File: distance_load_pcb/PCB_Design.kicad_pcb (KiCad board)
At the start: 2 copper layers, 14 parts, among them J1 From Power Source 5V, J2 From Limit Switch (LS), J3 From Encoder (EC), J5 Screen_Front, J6 Screen_Back, J7 From Load Cell (LC), U1 ESP-01v090, U2 YAAJ_BluePill_Part_Like_SWD_B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

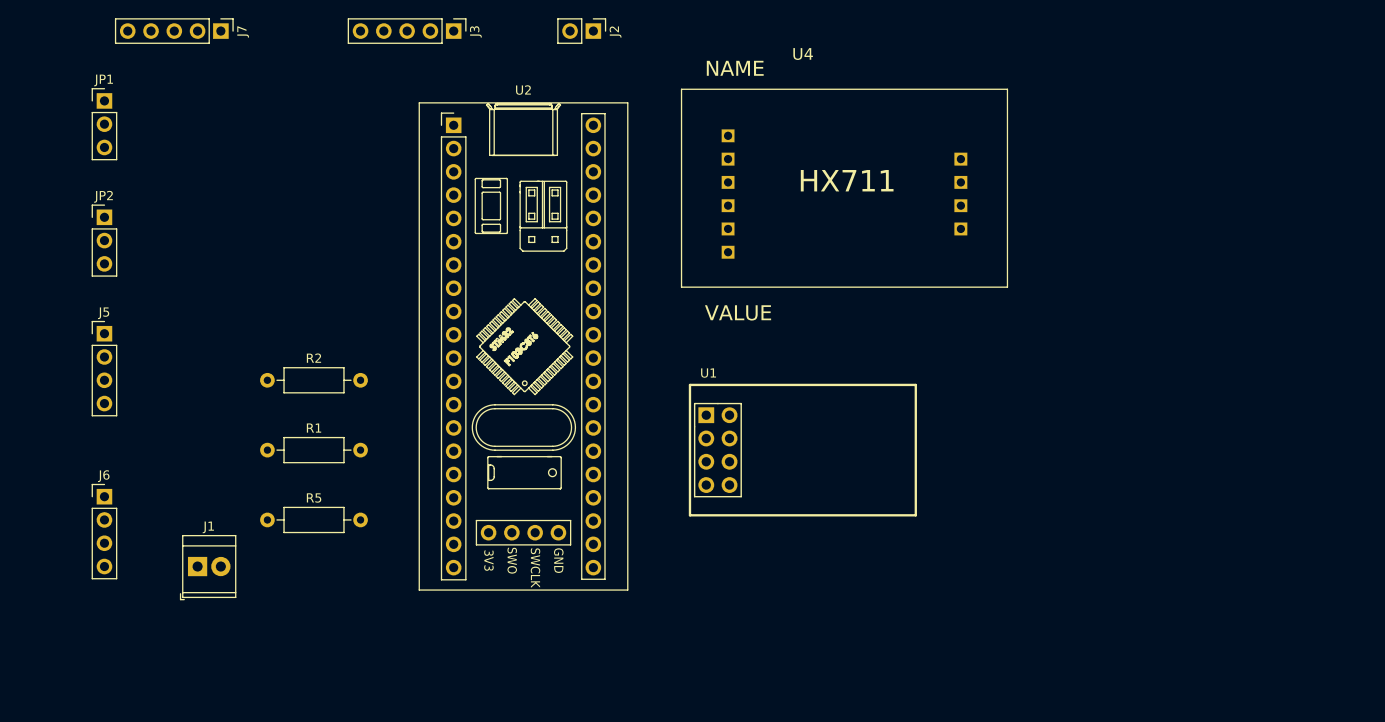
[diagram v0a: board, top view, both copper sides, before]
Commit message: finish pcb force and distance
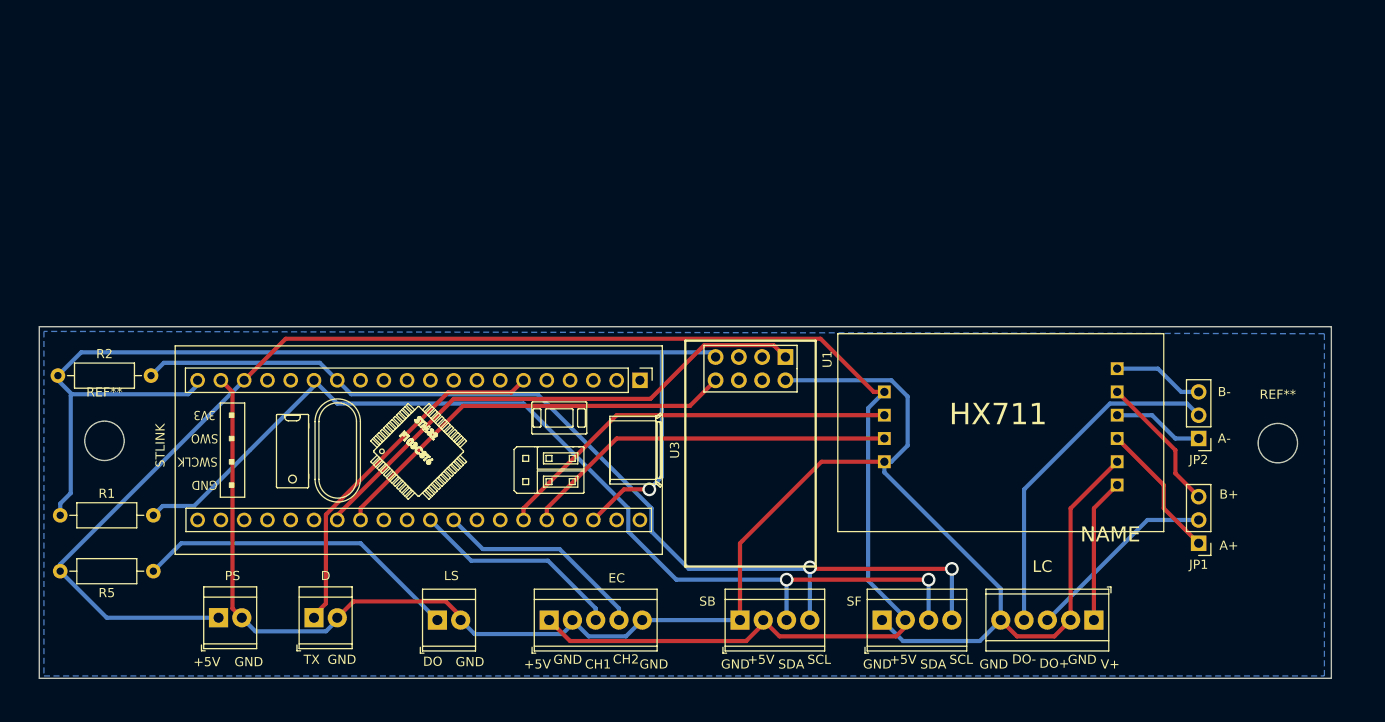
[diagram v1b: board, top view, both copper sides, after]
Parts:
- removed U2: YAAJ_BluePill_Part_Like_SWD_Breakout, Footprints:YAAJ_BluePill_SWD_1
- added D: Debug output, TerminalBlock_TE-Connectivity:TerminalBlock_TE_282834-2_1x02_P2.54mm_Horizontal, F.Cu at (99.1, 99.6)
- added REF**: MountingHole_4.3mm_M4, MountingHole:MountingHole_4.3mm_M4, F.Cu at (204.2, 80.5)
- added REF**: MountingHole_4.3mm_M4, MountingHole:MountingHole_4.3mm_M4, F.Cu at (76.2, 80.3)
- added U3: YAAJ_BluePill_Part_Like, Footprints:YAAJ_BluePill_1, F.Cu at (134.6, 73.7)
- EC: renamed from J3; footprint Connector_PinHeader_2.54mm:PinHeader_1x05_P2.54mm_Vertical -> TerminalBlock_TE-Connectivity:TerminalBlock_TE_282834-5_1x05_P2.54mm_Horizontal
- J7: footprint Connector_PinHeader_2.54mm:PinHeader_1x05_P2.54mm_Vertical -> TerminalBlock_TE-Connectivity:TerminalBlock_TE_282834-5_1x05_P2.54mm_Horizontal
- LS: renamed from J2; footprint Connector_PinHeader_2.54mm:PinHeader_1x02_P2.54mm_Vertical -> TerminalBlock_TE-Connectivity:TerminalBlock_TE_282834-2_1x02_P2.54mm_Horizontal
- SB: renamed from J6; footprint Connector_PinHeader_2.54mm:PinHeader_1x04_P2.54mm_Vertical -> TerminalBlock_TE-Connectivity:TerminalBlock_TE_282834-4_1x04_P2.54mm_Horizontal
- SF: renamed from J5; footprint Connector_PinHeader_2.54mm:PinHeader_1x04_P2.54mm_Vertical -> TerminalBlock_TE-Connectivity:TerminalBlock_TE_282834-4_1x04_P2.54mm_Horizontal
- moved JP1 128.8 mm to (195.6, 91.4), turned to 180 degrees
- moved JP2 121.8 mm to (195.6, 80.0), turned to 180 degrees
- moved J7 114.9 mm to (184.2, 99.8), turned to 180 degrees
- moved SF 90.4 mm to (161.0, 99.8)
- moved SB 70.6 mm to (145.5, 99.8)
- moved LS 66.5 mm to (112.5, 99.8), turned to 0 degrees
- moved EC 65.1 mm to (124.7, 99.8), turned to 0 degrees
- moved LC 63.6 mm to (195.6, 55.9), turned to 180 degrees
- moved R1 23.7 mm to (71.4, 88.4)
- moved R2 22.9 mm to (71.1, 73.2)
- moved R5 13.6 mm to (81.5, 94.5), turned to 180 degrees
- moved U1 10.7 mm to (150.5, 71.1), turned to -90 degrees
- moved PS 6.04 mm to (88.6, 99.6)
- renumbered U4 to LC, J1 to PS
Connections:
- net Shield_EC renamed GND
- EC pad 1: V+_EC -> +5V
- LC pad VCC: A_DEFINIR -> +5V
- U1 pad 1: USART1_TX -> USART2_TX
- U1 pad 8: USART1_RX -> USART2_RX
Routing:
- net GND: track 0.00 -> 203.7 mm
- net +5V: track 0.00 -> 192.9 mm
- net +3.3V: track 0.00 -> 127.1 mm, vias 0 -> 1
- net SDA1: track 0.00 -> 110.6 mm, vias 0 -> 2
- net SCL1: track 0.00 -> 110.2 mm, vias 0 -> 2
- net USART2_TX: track 0.00 -> 57.6 mm
- net USART2_RX: track 0.00 -> 45.8 mm
- net USART3_TX: track 0.00 -> 44.8 mm
- net USART3_RX: track 0.00 -> 41.3 mm
- net USART1_TX: track 0.00 -> 39.4 mm
- net DO-_LC: track 0.00 -> 38.2 mm
- net DO_LS: track 0.00 -> 35.7 mm
- net CH2-_EC: track 0.00 -> 23.3 mm
- net CH1_EC: track 0.00 -> 23.3 mm
- net DO+_LC: track 0.00 -> 21.0 mm
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- added copper zone on B.Cu, net GND
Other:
- board outline added: 141 x 38.4 mm
- board text added: "+5V"
- board text added: "A+"
- board text added: "A-"
- board text added: "B+"
- board text added: "B-"
- board text added: "CH1"
- board text added: "CH2"
- board text added: "DO"
- board text added: "DO+"
- board text added: "DO-"
- board text added: "GND"
- board text added: "SCL"
- board text added: "SDA"
- board text added: "STLINK"
- board text added: "TX"
- board text added: "V+"

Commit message: felipin's suggestions, all the tracs arrive at the components by the bottom
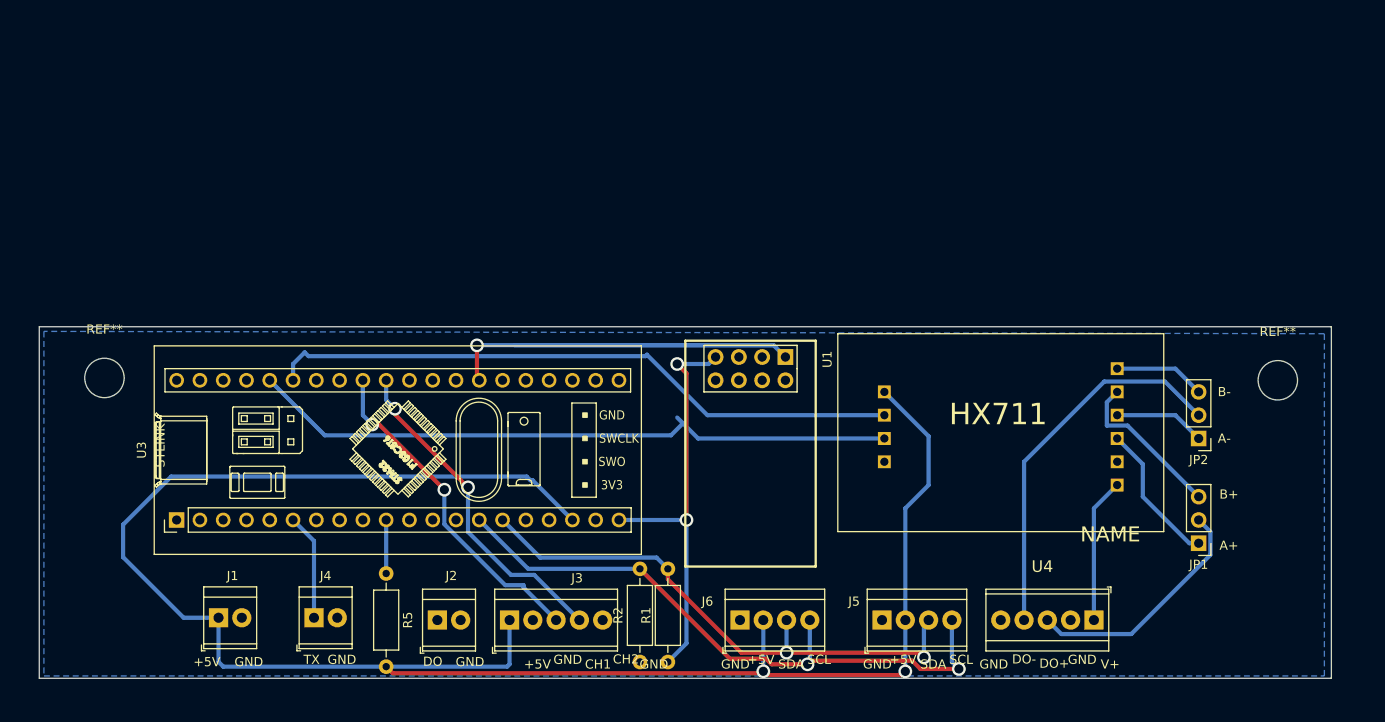
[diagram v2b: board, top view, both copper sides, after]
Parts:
- moved R2 70.8 mm to (134.6, 104.4), turned to 90 degrees
- moved R1 68.2 mm to (137.7, 104.4), turned to 90 degrees
- moved U3 52.8 mm to (84.1, 88.9), turned to 90 degrees
- moved R5 25.4 mm to (106.9, 94.7), turned to -90 degrees
- moved REF** 6.86 mm to (204.2, 73.7)
- moved REF** 6.86 mm to (76.2, 73.4)
- moved J3 4.32 mm to (120.4, 99.8)
- renumbered PS to J1, LS to J2, EC to J3, D to J4, SF to J5, SB to J6, LC to U4
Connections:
- J3 pad 3: CH1_EC -> CH2-_EC
- J3 pad 4: CH2-_EC -> CH1_EC
- U3 pad 10: unconnected-(U3-PA15-Pad10) -> DO_LS
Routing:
- net GND: track 203.7 -> 0.00 mm
- net +3.3V: track 127.1 -> 45.6 mm, vias 1 -> 2
- net SDA1: track 110.6 -> 60.7 mm
- net USART2_RX: track 45.8 -> 0.00 mm
- net SCL1: track 110.2 -> 70.0 mm
- net USART3_RX: track 41.3 -> 71.7 mm
- net DO_LS: track 35.7 -> 5.84 mm
- net USART1_TX: track 39.4 -> 11.6 mm
- net USART3_TX: track 44.8 -> 69.8 mm
- net +5V: track 192.9 -> 208.1 mm, vias 0 -> 2
- net CH2-_EC: track 23.3 -> 37.8 mm, vias 0 -> 2
- net CH1_EC: track 23.3 -> 36.4 mm, vias 0 -> 2
- net USART2_TX: track 57.6 -> 66.4 mm, vias 0 -> 1
- net DO+_LC: track 21.0 -> 26.3 mm
- net DO-_LC: track 38.2 -> 41.5 mm
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
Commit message: fix pcb
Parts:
- removed the REF** at (204.2, 73.7)
- removed the REF** at (76.2, 73.4)
- added REF**: MountingHole_4.3mm_M4, MountingHole:MountingHole_4.3mm_M4, F.Cu at (75.9, 72.1)
- added REF**: MountingHole_4.3mm_M4, MountingHole:MountingHole_4.3mm_M4, F.Cu at (204.0, 72.4)
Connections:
- U3 pad 10: DO_LS -> unconnected-(U3-PA15-Pad10)
- U3 pad 33: DO_Encoder -> DO_LS
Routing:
- net USART2_RX: track 0.00 -> 38.3 mm, vias 0 -> 1
- net DO_LS: track 5.84 -> 31.5 mm, vias 0 -> 2
- net USART2_TX: track 66.4 -> 41.3 mm
- net +3.3V: track 45.6 -> 48.7 mm
- net USART3_TX: track 69.8 -> 67.6 mm
- net USART3_RX: track 71.7 -> 69.7 mm
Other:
- board size 141 x 38.4 mm -> 141 x 41.9 mm

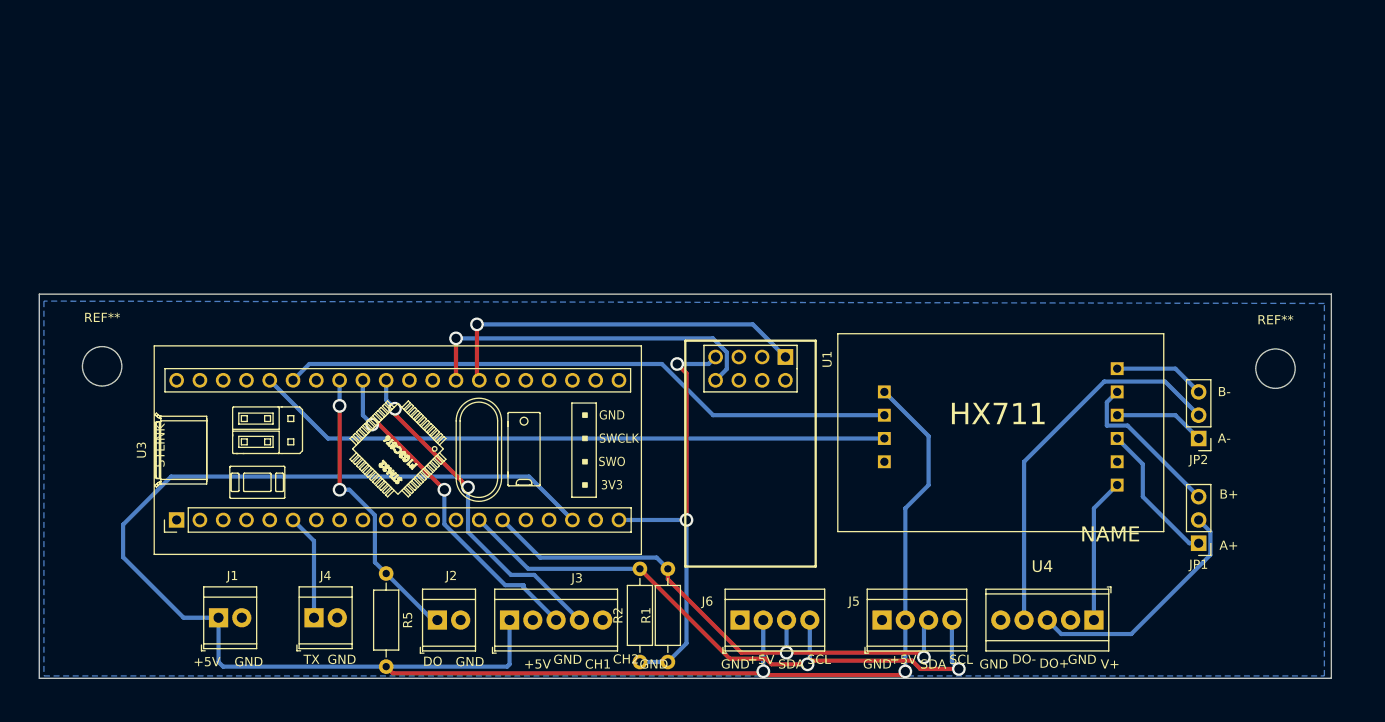
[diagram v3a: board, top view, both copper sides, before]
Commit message: solid gnd plane, added solsticio to the side
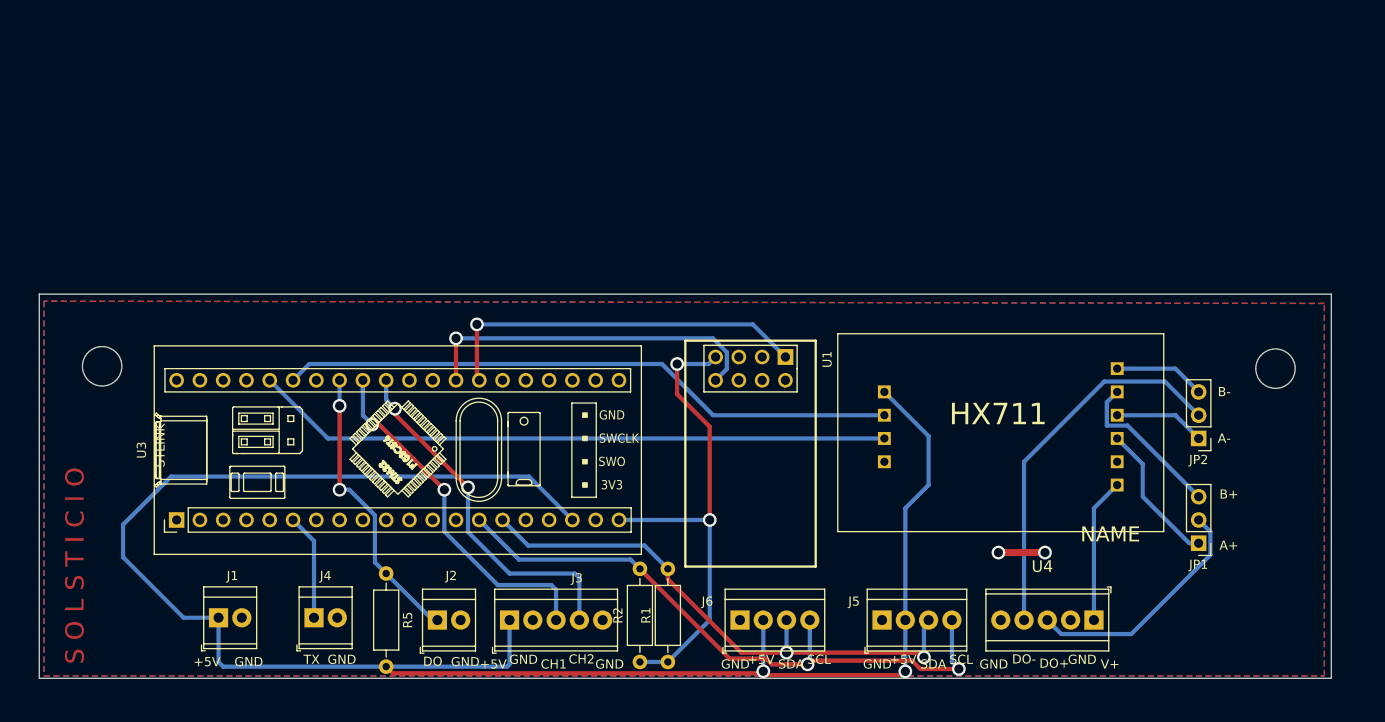
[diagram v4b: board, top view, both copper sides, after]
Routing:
- net GND: track 0.00 -> 5.59 mm, vias 0 -> 2
- net +3.3V: track 48.7 -> 53.3 mm
- net CH1_EC: track 36.4 -> 39.1 mm
- net CH2-_EC: track 37.8 -> 40.0 mm
- added copper zone on F.Cu, net GND
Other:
- board text added: "S O L S T I C I O"

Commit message: Vamos Solsticio!
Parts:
- removed REF** (x2): MountingHole_4.3mm_M4, MountingHole:MountingHole_4.3mm_M4
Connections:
- J7 pad 3: DO+_LC -> DO-_LC
- J7 pad 4: DO-_LC -> DO+_LC
- JP1 pad 1: A+ -> A-
- JP1 pad 2: DO+_LC -> DO-_LC
- JP1 pad 3: B+ -> B-
- JP2 pad 1: A- -> A+
- JP2 pad 2: DO-_LC -> DO+_LC
- JP2 pad 3: B- -> B+
- U4 pad A+: A- -> A+
- U4 pad A-: A+ -> A-
- U4 pad B+: B- -> B+
- U4 pad B-: B+ -> B-
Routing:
- net DO-_LC: track 41.5 -> 26.3 mm
- net DO+_LC: track 26.3 -> 41.5 mm
- net B-: track 9.94 -> 17.4 mm
- net B+: track 17.4 -> 9.94 mm
- net A-: track 9.94 -> 15.7 mm
- net A+: track 15.7 -> 9.94 mm
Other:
- board text added: "BS"
- board text added: "DB"
- board text added: "EC"
- board text added: "FS"
- board text added: "LS"
- board text added: "POW"

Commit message: last revision of the distance_load, printed
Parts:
- added REF**: MountingHole_4.3mm_M4, MountingHole:MountingHole_4.3mm_M4, F.Cu at (204.0, 72.4)
- added REF**: MountingHole_4.3mm_M4, MountingHole:MountingHole_4.3mm_M4, F.Cu at (75.9, 72.1)
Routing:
- net SDA1: track 60.7 -> 73.2 mm
- net GND: track 5.59 -> 15.8 mm
- net SCL1: track 70.0 -> 74.4 mm
- net +5V: track 208.1 -> 206.1 mm
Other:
- board text added: "Encoder"
- board text removed: "EC"
